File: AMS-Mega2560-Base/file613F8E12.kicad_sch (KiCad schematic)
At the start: 8 parts, among them IC21 MAX31865AAP+, J27 Conn_01x02, J28 Conn_01x03, J29 Conn_01x02

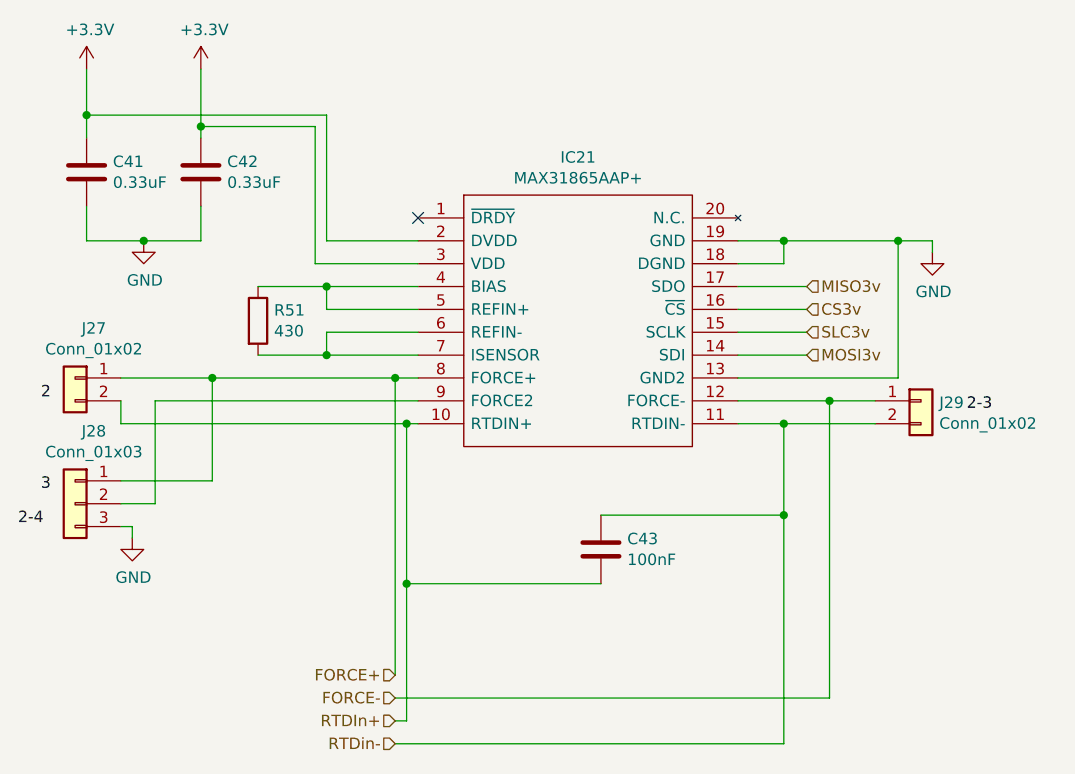
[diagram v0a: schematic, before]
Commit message: fixing some library settings and updating some schematics
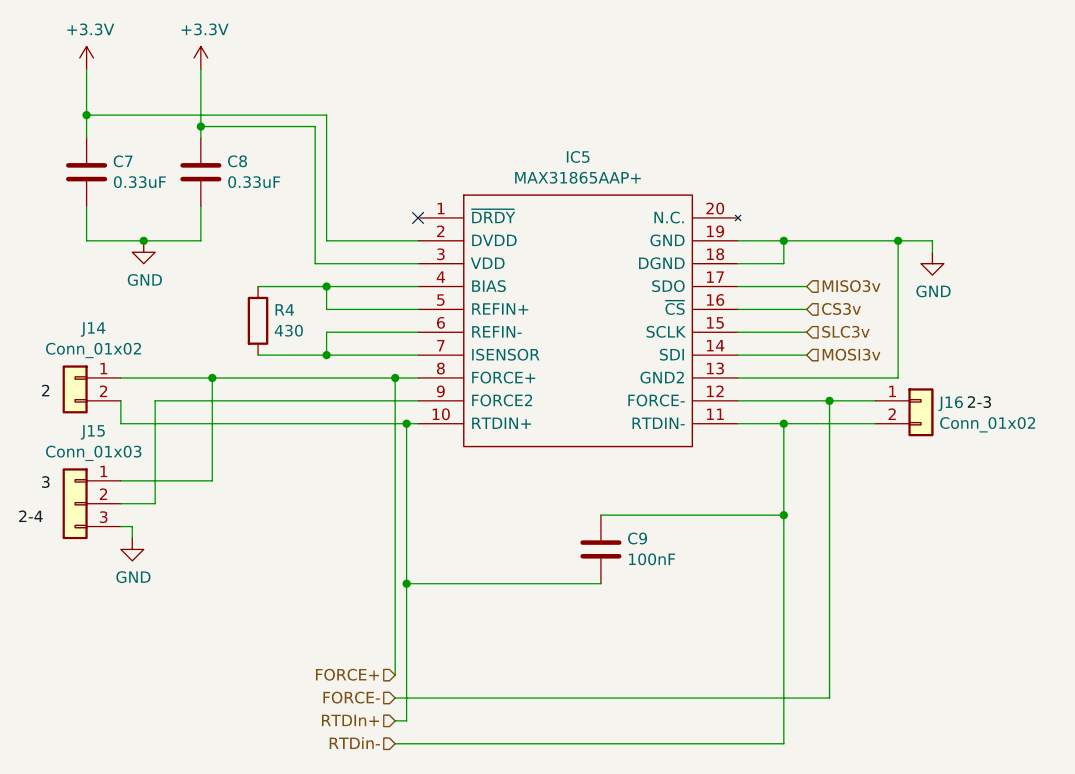
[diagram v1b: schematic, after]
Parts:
- R4: renamed from R51; footprint Resistor_THT:R_Axial_DIN0207_L6.3mm_D2.5mm_P5.08mm_Vertical -> Resistor_THT:R_Axial_DIN0207_L6.3mm_D2.5mm_P2.54mm_Vertical
- renumbered C41 to C7, C42 to C8, C43 to C9, IC21 to IC5, J27 to J14, J28 to J15, J29 to J16
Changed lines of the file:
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@@
   (symbol (lib_id "SamacSys_Parts:MAX31865AAP+") (at 135.89 77.47 0)
     (in_bom yes) (on_board yes)
-    (property "Reference" "IC21" (id 0) (at 153.67 70.739 0))
+    (property "Reference" "IC5" (id 0) (at 153.67 70.739 0))
     (property "Value" "MAX31865AAP+" (id 1) (at 153.67 73.0504 0))
     (property "Footprint" "SamacSys_Parts:SOP65P778X199-20N" (id 2) (at 167.64 74.93 0)
@@
   (symbol (lib_id "power:GND") (at 193.04 81.28 0)
     (in_bom yes) (on_board yes)
-    (property "Reference" "#PWR0124" (id 0) (at 193.04 87.63 0)
+    (property "Reference" "#PWR034" (id 0) (at 193.04 87.63 0)
       (effects (font (size 1.27 1.27)) hide)
     )
@@
   (symbol (lib_id "power:+3.3V") (at 99.06 60.96 0)
     (in_bom yes) (on_board yes)
-    (property "Reference" "#PWR0120" (id 0) (at 99.06 64.77 0)
+    (property "Reference" "#PWR030" (id 0) (at 99.06 64.77 0)
       (effects (font (size 1.27 1.27)) hide)
     )
@@
   (symbol (lib_id "Device:C") (at 111.76 72.39 0)
     (in_bom yes) (on_board yes)
-    (property "Reference" "C42" (id 0) (at 114.681 71.2216 0)
+    (property "Reference" "C8" (id 0) (at 114.681 71.2216 0)
       (effects (font (size 1.27 1.27)) (justify left))
     )
@@
   (symbol (lib_id "Device:C") (at 99.06 72.39 0)
     (in_bom yes) (on_board yes)
-    (property "Reference" "C41" (id 0) (at 101.981 71.2216 0)
+    (property "Reference" "C7" (id 0) (at 101.981 71.2216 0)
       (effects (font (size 1.27 1.27)) (justify left))
     )
@@
   (symbol (lib_id "power:GND") (at 105.41 80.01 0)
     (in_bom yes) (on_board yes)
-    (property "Reference" "#PWR0122" (id 0) (at 105.41 86.36 0)
+    (property "Reference" "#PWR032" (id 0) (at 105.41 86.36 0)
       (effects (font (size 1.27 1.27)) hide)
     )
@@
   (symbol (lib_id "Device:R") (at 118.11 88.9 0)
     (in_bom yes) (on_board yes)
-    (property "Reference" "R51" (id 0) (at 119.888 87.7316 0)
+    (property "Reference" "R4" (id 0) (at 119.888 87.7316 0)
       (effects (font (size 1.27 1.27)) (justify left))
     )
@@
       (effects (font (size 1.27 1.27)) (justify left))
     )
-    (property "Footprint" "Resistor_THT:R_Axial_DIN0207_L6.3mm_D2.5mm_P5.08mm_Vertical" (id 2) (at 116.332 88.9 90)
+    (property "Footprint" "Resistor_THT:R_Axial_DIN0207_L6.3mm_D2.5mm_P2.54mm_Vertical" (id 2) (at 116.332 88.9 90)
       (effects (font (size 1.27 1.27)) hide)
     )
@@
   (symbol (lib_id "power:GND") (at 104.14 113.03 0)
     (in_bom yes) (on_board yes)
-    (property "Reference" "#PWR0121" (id 0) (at 104.14 119.38 0)
+    (property "Reference" "#PWR031" (id 0) (at 104.14 119.38 0)
       (effects (font (size 1.27 1.27)) hide)
     )
@@
   (symbol (lib_id "power:+3.3V") (at 111.76 60.96 0)
     (in_bom yes) (on_board yes)
-    (property "Reference" "#PWR0123" (id 0) (at 111.76 64.77 0)
+    (property "Reference" "#PWR033" (id 0) (at 111.76 64.77 0)
       (effects (font (size 1.27 1.27)) hide)
     )
@@
   (symbol (lib_id "Connector_Generic:Conn_01x02") (at 97.79 95.25 0) (mirror y)
     (in_bom yes) (on_board yes)
-    (property "Reference" "J27" (id 0) (at 99.8728 89.7382 0))
+    (property "Reference" "J14" (id 0) (at 99.8728 89.7382 0))
     (property "Value" "Conn_01x02" (id 1) (at 99.8728 92.0496 0))
     (property "Footprint" "Connector_PinHeader_2.54mm:PinHeader_1x02_P2.54mm_Vertical" (id 2) (at 97.79 95.25 0)
@@
   (symbol (lib_id "Connector_Generic:Conn_01x03") (at 97.79 109.22 0) (mirror y)
     (in_bom yes) (on_board yes)
-    (property "Reference" "J28" (id 0) (at 99.8728 101.1682 0))
+    (property "Reference" "J15" (id 0) (at 99.8728 101.1682 0))
     (property "Value" "Conn_01x03" (id 1) (at 99.8728 103.4796 0))
     (property "Footprint" "Connector_PinHeader_2.54mm:PinHeader_1x03_P2.54mm_Vertical" (id 2) (at 97.79 109.22 0)
@@
   (symbol (lib_id "Connector_Generic:Conn_01x02") (at 191.77 97.79 0)
     (in_bom yes) (on_board yes)
-    (property "Reference" "J29" (id 0) (at 193.802 97.9932 0)
+    (property "Reference" "J16" (id 0) (at 193.802 97.9932 0)
       (effects (font (size 1.27 1.27)) (justify left))
     )
@@
   (symbol (lib_id "Device:C") (at 156.21 114.3 0)
     (in_bom yes) (on_board yes)
-    (property "Reference" "C43" (id 0) (at 159.131 113.1316 0)
-      (effects (font (size 1.27 1.27)) (justify left))
-    )
+    (property "Reference" "C9" (id 0) (at 159.131 113.1316 0)
+      (effects (font (size 1.27 1.27)) (justify left))
+    )

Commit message: BaseBoard fixes and updates. doing schematic work.
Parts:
- renumbered C7 to C41, C8 to C42, C9 to C43, IC5 to IC18, J14 to J28, J15 to J29, J16 to J30, R4 to R60
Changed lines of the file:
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@@
   (symbol (lib_id "SamacSys_Parts:MAX31865AAP+") (at 135.89 77.47 0)
     (in_bom yes) (on_board yes)
-    (property "Reference" "IC5" (id 0) (at 153.67 70.739 0))
+    (property "Reference" "IC18" (id 0) (at 153.67 70.739 0))
     (property "Value" "MAX31865AAP+" (id 1) (at 153.67 73.0504 0))
     (property "Footprint" "SamacSys_Parts:SOP65P778X199-20N" (id 2) (at 167.64 74.93 0)
@@
   (symbol (lib_id "power:GND") (at 193.04 81.28 0)
     (in_bom yes) (on_board yes)
-    (property "Reference" "#PWR034" (id 0) (at 193.04 87.63 0)
+    (property "Reference" "#PWR0120" (id 0) (at 193.04 87.63 0)
       (effects (font (size 1.27 1.27)) hide)
     )
@@
   (symbol (lib_id "power:+3.3V") (at 99.06 60.96 0)
     (in_bom yes) (on_board yes)
-    (property "Reference" "#PWR030" (id 0) (at 99.06 64.77 0)
+    (property "Reference" "#PWR0116" (id 0) (at 99.06 64.77 0)
       (effects (font (size 1.27 1.27)) hide)
     )
@@
   (symbol (lib_id "Device:C") (at 111.76 72.39 0)
     (in_bom yes) (on_board yes)
-    (property "Reference" "C8" (id 0) (at 114.681 71.2216 0)
+    (property "Reference" "C42" (id 0) (at 114.681 71.2216 0)
       (effects (font (size 1.27 1.27)) (justify left))
     )
@@
   (symbol (lib_id "Device:C") (at 99.06 72.39 0)
     (in_bom yes) (on_board yes)
-    (property "Reference" "C7" (id 0) (at 101.981 71.2216 0)
+    (property "Reference" "C41" (id 0) (at 101.981 71.2216 0)
       (effects (font (size 1.27 1.27)) (justify left))
     )
@@
   (symbol (lib_id "power:GND") (at 105.41 80.01 0)
     (in_bom yes) (on_board yes)
-    (property "Reference" "#PWR032" (id 0) (at 105.41 86.36 0)
+    (property "Reference" "#PWR0118" (id 0) (at 105.41 86.36 0)
       (effects (font (size 1.27 1.27)) hide)
     )
@@
   (symbol (lib_id "Device:R") (at 118.11 88.9 0)
     (in_bom yes) (on_board yes)
-    (property "Reference" "R4" (id 0) (at 119.888 87.7316 0)
+    (property "Reference" "R60" (id 0) (at 119.888 87.7316 0)
       (effects (font (size 1.27 1.27)) (justify left))
     )
@@
   (symbol (lib_id "power:GND") (at 104.14 113.03 0)
     (in_bom yes) (on_board yes)
-    (property "Reference" "#PWR031" (id 0) (at 104.14 119.38 0)
+    (property "Reference" "#PWR0117" (id 0) (at 104.14 119.38 0)
       (effects (font (size 1.27 1.27)) hide)
     )
@@
   (symbol (lib_id "power:+3.3V") (at 111.76 60.96 0)
     (in_bom yes) (on_board yes)
-    (property "Reference" "#PWR033" (id 0) (at 111.76 64.77 0)
+    (property "Reference" "#PWR0119" (id 0) (at 111.76 64.77 0)
       (effects (font (size 1.27 1.27)) hide)
     )
@@
   (symbol (lib_id "Connector_Generic:Conn_01x02") (at 97.79 95.25 0) (mirror y)
     (in_bom yes) (on_board yes)
-    (property "Reference" "J14" (id 0) (at 99.8728 89.7382 0))
+    (property "Reference" "J28" (id 0) (at 99.8728 89.7382 0))
     (property "Value" "Conn_01x02" (id 1) (at 99.8728 92.0496 0))
     (property "Footprint" "Connector_PinHeader_2.54mm:PinHeader_1x02_P2.54mm_Vertical" (id 2) (at 97.79 95.25 0)
@@
   (symbol (lib_id "Connector_Generic:Conn_01x03") (at 97.79 109.22 0) (mirror y)
     (in_bom yes) (on_board yes)
-    (property "Reference" "J15" (id 0) (at 99.8728 101.1682 0))
+    (property "Reference" "J29" (id 0) (at 99.8728 101.1682 0))
     (property "Value" "Conn_01x03" (id 1) (at 99.8728 103.4796 0))
     (property "Footprint" "Connector_PinHeader_2.54mm:PinHeader_1x03_P2.54mm_Vertical" (id 2) (at 97.79 109.22 0)
@@
   (symbol (lib_id "Connector_Generic:Conn_01x02") (at 191.77 97.79 0)
     (in_bom yes) (on_board yes)
-    (property "Reference" "J16" (id 0) (at 193.802 97.9932 0)
+    (property "Reference" "J30" (id 0) (at 193.802 97.9932 0)
       (effects (font (size 1.27 1.27)) (justify left))
     )
@@
   (symbol (lib_id "Device:C") (at 156.21 114.3 0)
     (in_bom yes) (on_board yes)
-    (property "Reference" "C9" (id 0) (at 159.131 113.1316 0)
-      (effects (font (size 1.27 1.27)) (justify left))
-    )
+    (property "Reference" "C43" (id 0) (at 159.131 113.1316 0)
+      (effects (font (size 1.27 1.27)) (justify left))
+    )

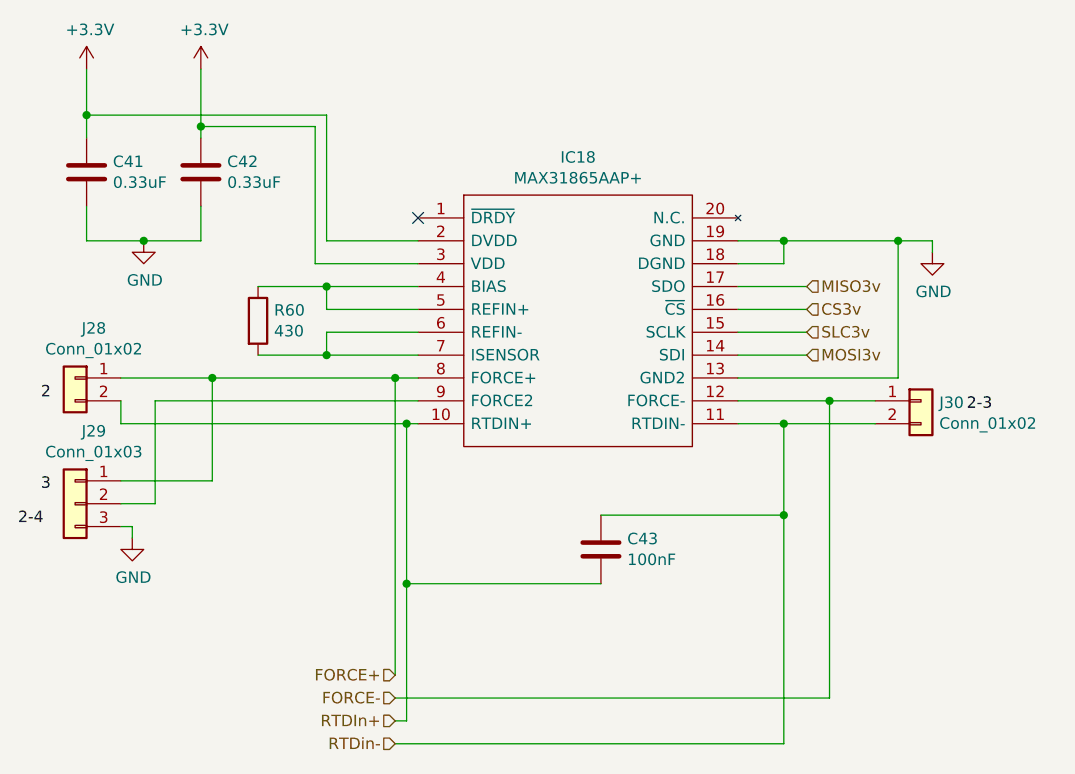
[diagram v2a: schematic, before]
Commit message: trying to fix the PCB layout.
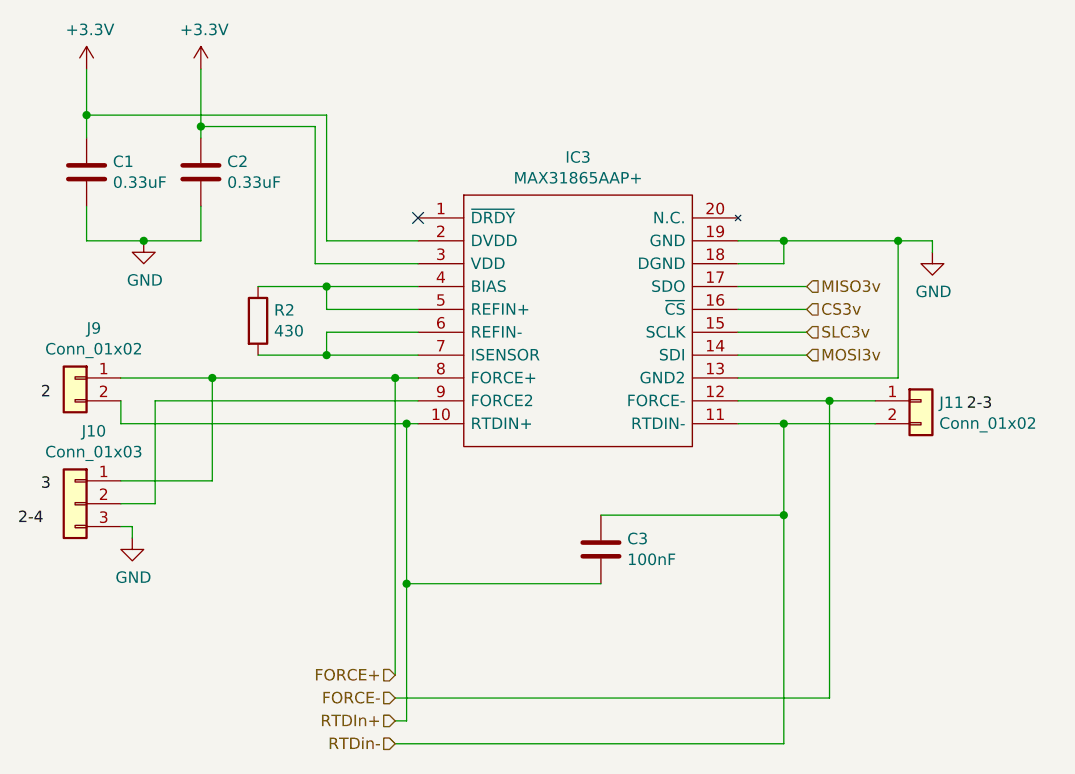
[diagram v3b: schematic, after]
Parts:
- renumbered C41 to C1, C42 to C2, C43 to C3, IC18 to IC3, J29 to J10, J30 to J11, J28 to J9, R60 to R2
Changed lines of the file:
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@@
   (symbol (lib_id "SamacSys_Parts:MAX31865AAP+") (at 135.89 77.47 0)
     (in_bom yes) (on_board yes)
-    (property "Reference" "IC18" (id 0) (at 153.67 70.739 0))
+    (property "Reference" "IC3" (id 0) (at 153.67 70.739 0))
     (property "Value" "MAX31865AAP+" (id 1) (at 153.67 73.0504 0))
     (property "Footprint" "SamacSys_Parts:SOP65P778X199-20N" (id 2) (at 167.64 74.93 0)
@@
   (symbol (lib_id "power:GND") (at 193.04 81.28 0)
     (in_bom yes) (on_board yes)
-    (property "Reference" "#PWR0120" (id 0) (at 193.04 87.63 0)
+    (property "Reference" "#PWR026" (id 0) (at 193.04 87.63 0)
       (effects (font (size 1.27 1.27)) hide)
     )
@@
   (symbol (lib_id "power:+3.3V") (at 99.06 60.96 0)
     (in_bom yes) (on_board yes)
-    (property "Reference" "#PWR0116" (id 0) (at 99.06 64.77 0)
+    (property "Reference" "#PWR022" (id 0) (at 99.06 64.77 0)
       (effects (font (size 1.27 1.27)) hide)
     )
@@
   (symbol (lib_id "Device:C") (at 111.76 72.39 0)
     (in_bom yes) (on_board yes)
-    (property "Reference" "C42" (id 0) (at 114.681 71.2216 0)
+    (property "Reference" "C2" (id 0) (at 114.681 71.2216 0)
       (effects (font (size 1.27 1.27)) (justify left))
     )
@@
   (symbol (lib_id "Device:C") (at 99.06 72.39 0)
     (in_bom yes) (on_board yes)
-    (property "Reference" "C41" (id 0) (at 101.981 71.2216 0)
+    (property "Reference" "C1" (id 0) (at 101.981 71.2216 0)
       (effects (font (size 1.27 1.27)) (justify left))
     )
@@
   (symbol (lib_id "power:GND") (at 105.41 80.01 0)
     (in_bom yes) (on_board yes)
-    (property "Reference" "#PWR0118" (id 0) (at 105.41 86.36 0)
+    (property "Reference" "#PWR024" (id 0) (at 105.41 86.36 0)
       (effects (font (size 1.27 1.27)) hide)
     )
@@
   (symbol (lib_id "Device:R") (at 118.11 88.9 0)
     (in_bom yes) (on_board yes)
-    (property "Reference" "R60" (id 0) (at 119.888 87.7316 0)
+    (property "Reference" "R2" (id 0) (at 119.888 87.7316 0)
       (effects (font (size 1.27 1.27)) (justify left))
     )
@@
   (symbol (lib_id "power:GND") (at 104.14 113.03 0)
     (in_bom yes) (on_board yes)
-    (property "Reference" "#PWR0117" (id 0) (at 104.14 119.38 0)
+    (property "Reference" "#PWR023" (id 0) (at 104.14 119.38 0)
       (effects (font (size 1.27 1.27)) hide)
     )
@@
   (symbol (lib_id "power:+3.3V") (at 111.76 60.96 0)
     (in_bom yes) (on_board yes)
-    (property "Reference" "#PWR0119" (id 0) (at 111.76 64.77 0)
+    (property "Reference" "#PWR025" (id 0) (at 111.76 64.77 0)
       (effects (font (size 1.27 1.27)) hide)
     )
@@
   (symbol (lib_id "Connector_Generic:Conn_01x02") (at 97.79 95.25 0) (mirror y)
     (in_bom yes) (on_board yes)
-    (property "Reference" "J28" (id 0) (at 99.8728 89.7382 0))
+    (property "Reference" "J9" (id 0) (at 99.8728 89.7382 0))
     (property "Value" "Conn_01x02" (id 1) (at 99.8728 92.0496 0))
     (property "Footprint" "Connector_PinHeader_2.54mm:PinHeader_1x02_P2.54mm_Vertical" (id 2) (at 97.79 95.25 0)
@@
   (symbol (lib_id "Connector_Generic:Conn_01x03") (at 97.79 109.22 0) (mirror y)
     (in_bom yes) (on_board yes)
-    (property "Reference" "J29" (id 0) (at 99.8728 101.1682 0))
+    (property "Reference" "J10" (id 0) (at 99.8728 101.1682 0))
     (property "Value" "Conn_01x03" (id 1) (at 99.8728 103.4796 0))
     (property "Footprint" "Connector_PinHeader_2.54mm:PinHeader_1x03_P2.54mm_Vertical" (id 2) (at 97.79 109.22 0)
@@
   (symbol (lib_id "Connector_Generic:Conn_01x02") (at 191.77 97.79 0)
     (in_bom yes) (on_board yes)
-    (property "Reference" "J30" (id 0) (at 193.802 97.9932 0)
+    (property "Reference" "J11" (id 0) (at 193.802 97.9932 0)
       (effects (font (size 1.27 1.27)) (justify left))
     )
@@
   (symbol (lib_id "Device:C") (at 156.21 114.3 0)
     (in_bom yes) (on_board yes)
-    (property "Reference" "C43" (id 0) (at 159.131 113.1316 0)
-      (effects (font (size 1.27 1.27)) (justify left))
-    )
+    (property "Reference" "C3" (id 0) (at 159.131 113.1316 0)
+      (effects (font (size 1.27 1.27)) (justify left))
+    )
